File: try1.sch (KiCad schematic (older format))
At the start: 15 parts, among them J10 Archon-connector-modules-Driv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, J11 Archon-connector-modules-Driv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, J2 Archon-connector-modules-Heat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, J21 DB37, J22 DB37, J3 Archon-connector-modules-Driv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, J31 DB9, J4 Archon-connector-modules-LVBi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, J5 Archon-connector-modules-ADC, J6 Archon-connector-modules-ADC, J7 Archon-connector-modules-ADC, J8 Archon-connector-modules-ADC, J9 Archon-connector-modules-HVBi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

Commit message: Finish version 31
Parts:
- gave numbers to parts that had none: 2
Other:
- note added: "Heater"
- note added: "Radiation Shield"
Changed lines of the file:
@@
 $EndComp
 $Comp
-L RJ45_LEDS_SHLD J?
+L RJ45_LEDS_SHLD J41
 U 1 1 5792318E
 P 12800 3250
-F 0 "J?" H 12800 2750 50  0000 C CNN
+F 0 "J41" H 12800 2750 50  0000 C CNN
 F 1 "RJ45_LEDS_SHLD" H 12800 3650 50  0000 C CNN
 F 2 "" H 12800 3200 50  0000 C CNN
@@
 $EndComp
 $Comp
-L RJ45_LEDS_SHLD J?
+L RJ45_LEDS_SHLD J42
 U 1 1 57923203
 P 14900 3250
-F 0 "J?" H 14900 2750 50  0000 C CNN
+F 0 "J42" H 14900 2750 50  0000 C CNN
 F 1 "RJ45_LEDS_SHLD" H 14900 3650 50  0000 C CNN
 F 2 "" H 14900 3200 50  0000 C CNN
@@
 Text Notes 2050 4150 0    60   ~ 0
 LED/Projector
+Text Notes 13700 4200 0    60   ~ 0
+Heater
+Text Notes 13700 4400 0    60   ~ 0
+Radiation Shield
 $EndSCHEMATC

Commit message: Incomplete Wireing (v39)
Switched out RJ45 connectors for DVI.

Partially completed connections.
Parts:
- removed J41, J42: RJ45_LEDS_SHLD, symbol RJ45_LEDS_SHLD
- added J41: CONN_DVI, MODULE, symbol CONN_DVI
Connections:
- net labels added: DRV10_CH1, DRV10_CH2, DRV10_CH3, DRV10_CH4, DRV10_CH5, DRV10_CH6, DRV10_CH7, DRV10_CH8, DRV11_CH1, DRV11_CH2, DRV11_CH3, DRV11_CH4, DRV11_CH5, DRV11_CH6, DRV11_CH7, DRV11_CH8, DRV3_CH1, DRV3_CH2, DRV3_CH3, DRV3_CH4, DRV3_CH5, DRV3_CH6, DRV3_CH7, DRV3_CH8, OUT_LL_GND, OUT_LR_GND, OUT_UL_GND, OUT_UR_GND, OUT__UL_GND
- wire segments 66 -> 92
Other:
- moved on the sheet: J10, J11, J2, J21, J22, J3, J31, J4, J5, J6, J7, J8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

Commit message: Version 41: Partial Wiring
Still very incomplete, but I finished the first pass on wiring.  This
version includes Morley's first pin assignments and some extra changes
we talked about, today.
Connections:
- net labels added: HV9_1, HV9_10, HV9_2, HV9_3, HV9_4, HV9_5, HV9_6, HV9_7, HV9_8, HV9_9, LV4_1, LV4_2, LV4_3, LV4_4, LV4_5, LV4_6, LV4_7, LV4_8, ResetLog_L, ResetLog_R
- net labels removed: ResetLOG_L, ResetLOG_R
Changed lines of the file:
@@
 Title "Archon CCD Camera Controller Interface Board"
 Date "2016-07-08"
-Rev "39"
+Rev "41"
 Comp "Porltand State University"
 Comment1 "Copyright 2016 Paul R. DeStefano"
@@
 ResetHI_L
 Text Label 15450 5300 0    60   ~ 0
-ResetLOG_L
+ResetLog_L
 Text Label 15450 5400 0    60   ~ 0
 VDD_B
@@
 ResetHI_R
 Text Label 12150 5300 0    60   ~ 0
-ResetLOG_R
+ResetLog_R
 Text Label 12150 5400 0    60   ~ 0
 VDD_A
@@
 Text GLabel 12750 3500 2    60   Input ~ 0
 DRV3_CH2
+Text GLabel 22300 11300 0    60   Input ~ 0
+HV9_5
+Text GLabel 22300 11400 0    60   Input ~ 0
+HV9_6
+Text GLabel 22300 11600 0    60   Input ~ 0
+HV9_7
+Text GLabel 22300 11700 0    60   Input ~ 0
+HV9_8
+Text GLabel 22300 11000 0    60   Input ~ 0
+HV9_3
+Text GLabel 22300 11100 0    60   Input ~ 0
+HV9_4
+Text GLabel 22300 10700 0    60   Input ~ 0
+HV9_1
+Text GLabel 22300 10800 0    60   Input ~ 0
+HV9_2
+Text GLabel 16350 5400 2    60   Input ~ 0
+HV9_1
+Text GLabel 16350 5700 2    60   Input ~ 0
+HV9_3
+Text GLabel 16350 5800 2    60   Input ~ 0
+HV9_5
+Text GLabel 16350 6000 2    60   Input ~ 0
+HV9_5
+Text GLabel 12750 5400 2    60   Input ~ 0
+HV9_2
+Text GLabel 12750 5700 2    60   Input ~ 0
+HV9_4
+Text GLabel 12750 5800 2    60   Input ~ 0
+HV9_6
+Text GLabel 12750 6000 2    60   Input ~ 0
+HV9_6
+Text GLabel 12750 5200 2    60   Input ~ 0
+HV9_8
+Text GLabel 16350 5200 2    60   Input ~ 0
+HV9_7
+Text GLabel 8600 10750 0    60   Input ~ 0
+LV4_1
+Text GLabel 8600 10850 0    60   Input ~ 0
+LV4_2
+Text GLabel 8600 11050 0    60   Input ~ 0
+LV4_3
+Text GLabel 8600 11150 0    60   Input ~ 0
+LV4_4
+Text GLabel 8600 11350 0    60   Input ~ 0
+LV4_5
+Text GLabel 8600 11450 0    60   Input ~ 0
+LV4_6
+Text GLabel 8600 11650 0    60   Input ~ 0
+LV4_7
+Text GLabel 8600 11750 0    60   Input ~ 0
+LV4_8
+Text GLabel 16350 5900 2    60   Input ~ 0
+LV4_1
+Text GLabel 12750 5900 2    60   Input ~ 0
+LV4_2
+Text GLabel 16350 5300 2    60   Input ~ 0
+DRV10_CH1
+Text GLabel 12750 5300 2    60   Input ~ 0
+DRV10_CH2
+Text GLabel 16350 4300 2    60   Input ~ 0
+DRV3_CH1
+Text GLabel 12750 4300 2    60   Input ~ 0
+DRV3_CH2
+Text GLabel 16350 4500 2    60   Input ~ 0
+DRV3_CH3
+Text GLabel 12750 4500 2    60   Input ~ 0
+DRV3_CH4
+Text GLabel 16350 4700 2    60   Input ~ 0
+DRV3_CH5
+Text GLabel 12750 4700 2    60   Input ~ 0
+DRV3_CH6
+Text GLabel 16350 4900 2    60   Input ~ 0
+DRV3_CH7
+Text GLabel 12750 4900 2    60   Input ~ 0
+DRV3_CH8
+Text GLabel 16350 6200 2    60   Input ~ 0
+HV9_9
+Text GLabel 12750 6200 2    60   Input ~ 0
+HV9_10
+Text GLabel 22300 11900 0    60   Input ~ 0
+HV9_9
+Text GLabel 22300 12000 0    60   Input ~ 0
+HV9_10
 $EndSCHEMATC

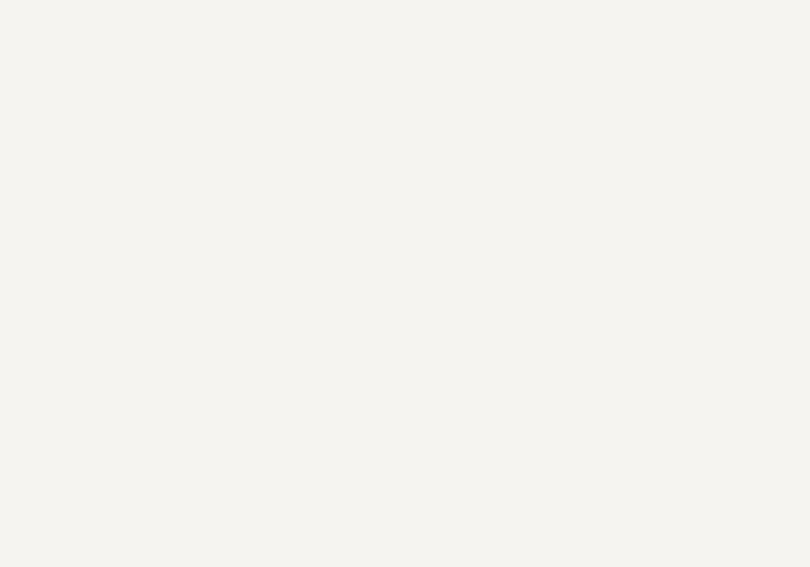
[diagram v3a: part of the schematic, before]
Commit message: Add heater power connector
Added Mini-FiT-Jr 5566 2x2 footprint and connector to hold heater power
connections to cold finger heater and radiation shield heater.
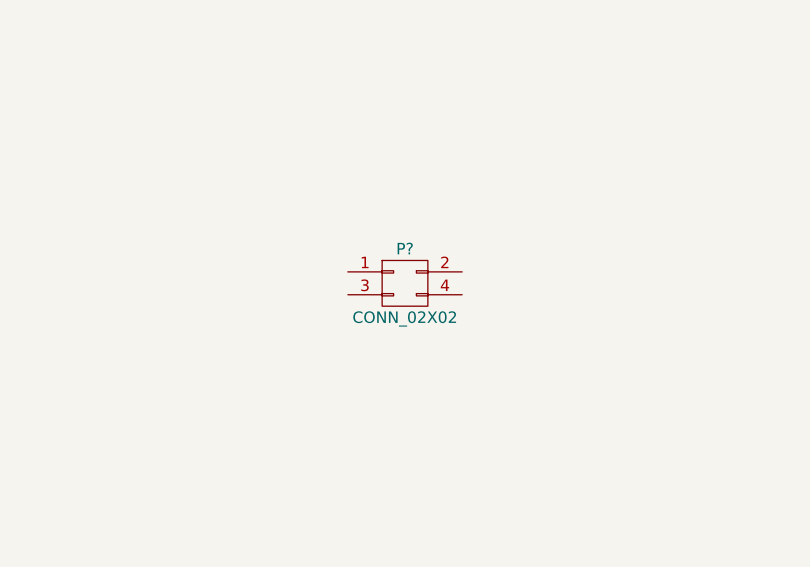
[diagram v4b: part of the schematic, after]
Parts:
- added P?: CONN_02X02, symbol CONN_02X02
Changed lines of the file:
@@
 Text GLabel 22300 12000 0    60   Input ~ 0
 HV9_10
+$Comp
+L CONN_02X02 P?
+U 1 1 57B547B3
+P 20850 4650
+F 0 "P?" H 20850 4800 50  0000 C CNN
+F 1 "CONN_02X02" H 20850 4500 50  0000 C CNN
+F 2 "" H 20850 3450 50  0000 C CNN
+F 3 "" H 20850 3450 50  0000 C CNN
+	1    20850 4650
+	1    0    0    -1
+$EndComp
 $EndSCHEMATC

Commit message: Connect heater/DVI, label shutter connector
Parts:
- added W? (x6): TEST_1P, symbol TEST_1P
- P?: footprint (none) -> ccdcamera:Molex_MiniFit-JR-5556-04B_2x02x4.20mm_Straight
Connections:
- net labels added: DVI_P9_SPARET1, DVI_P9_SPARET2, DVI_P9_SPARET3, DVI_P9_SPARET4, DVI_P9_SPARET5, DVI_P9_SPARET6, DVI_P9_T1, DVI_P9_T2, DVI_P9_T3, DVI_P9_T4, DVI_P9_T5, DVI_P9_T6, FLASH_V, HEATER1_AN, HEATER1_AP, HEATER1_BN, HEATER1_BP, HEATER1_TEMPA_FN, HEATER1_TEMPA_FP, HEATER1_TEMPA_SN, HEATER1_TEMPA_SP, HEATER1_TEMPB_FN, HEATER1_TEMPB_FP, HEATER1_TEMPB_SN, HEATER1_TEMPB_SP, SEL_LED_1, SEL_LED_2, SHUT_+15V, SHUT_+5, SHUT_OUT, ~FLASH_STB
- net labels removed: OUT__UL_GND
- wire segments 92 -> 66
- no-connect marks 26 -> 43
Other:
- note added: "LED/Projector\n(Formerly J73 - Shutter Control)"
- note added: "SHIELD PINS:\n3,11,19,22"
- note removed: "LED/Projector"

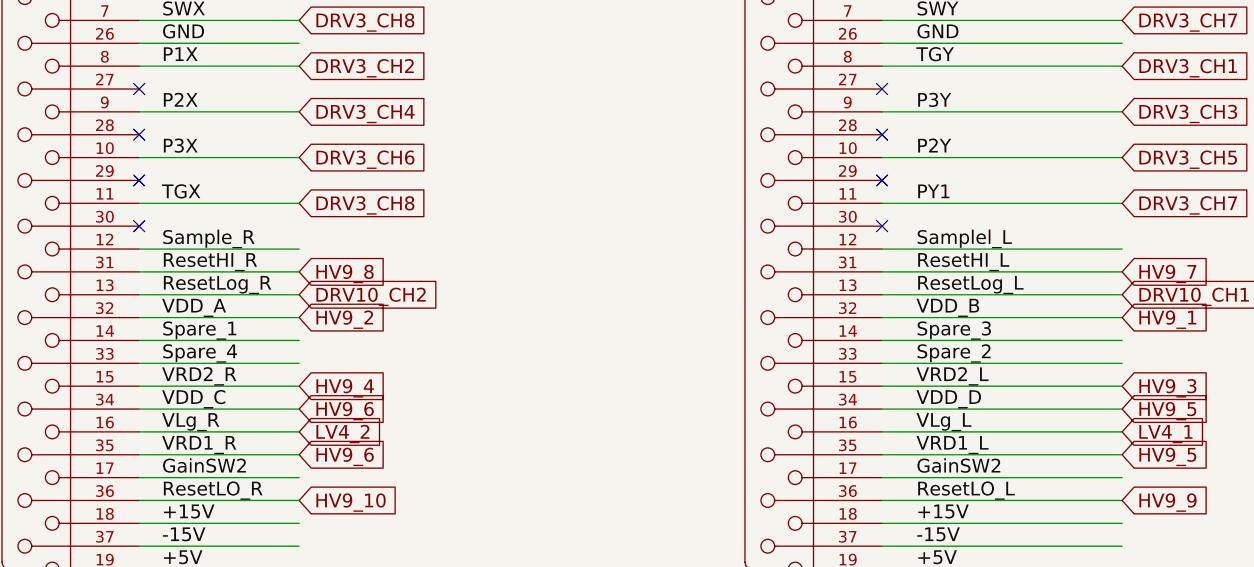
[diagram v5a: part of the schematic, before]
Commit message: schematic: chg ResetHI_L/R to ~(not) logic
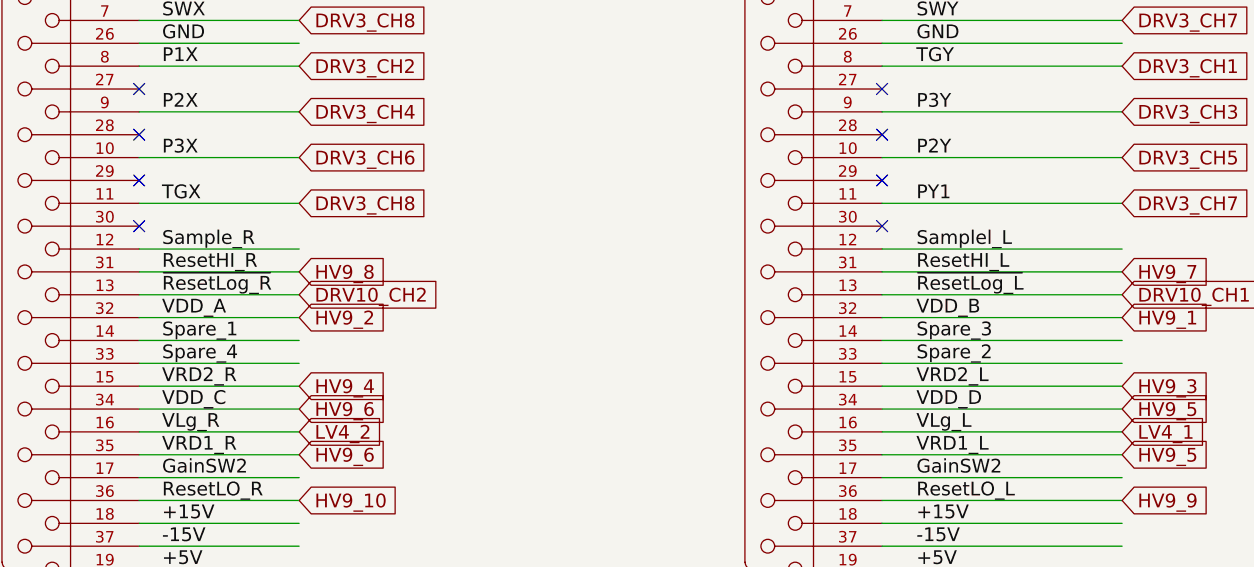
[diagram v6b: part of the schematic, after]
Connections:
- net labels added: ~ResetLog_L, ~ResetLog_R
- net labels removed: ResetLog_L, ResetLog_R
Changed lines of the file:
@@
 ResetHI_L
 Text Label 15450 5300 0    60   ~ 0
-ResetLog_L
+~ResetLog_L
 Text Label 15450 5400 0    60   ~ 0
 VDD_B
@@
 ResetHI_R
 Text Label 12150 5300 0    60   ~ 0
-ResetLog_R
+~ResetLog_R
 Text Label 12150 5400 0    60   ~ 0
 VDD_A

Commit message: fill with non-connects
Added non-connect flags for all unassinged pins.
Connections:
- net labels added: DRV3_GND1, DRV3_GND2
- no-connect marks 43 -> 310
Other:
- moved on the sheet: J7, J8

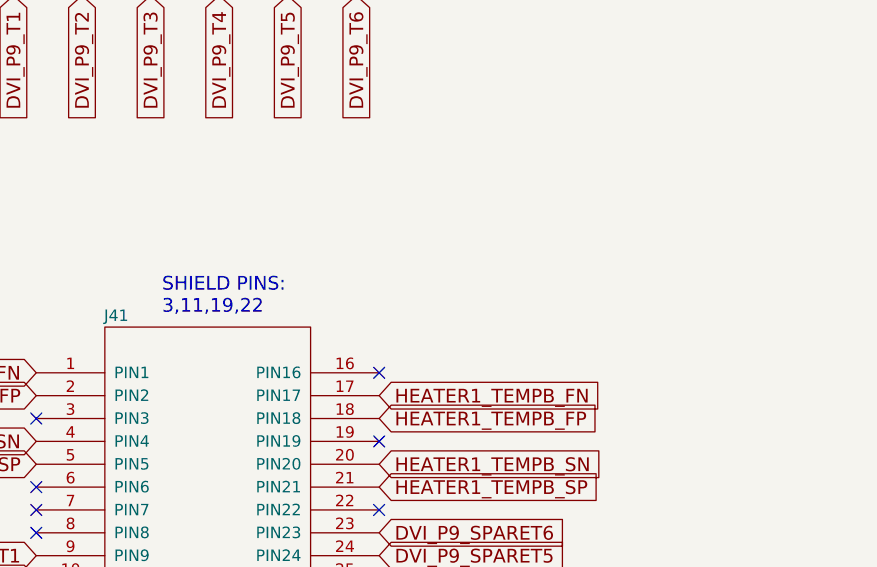
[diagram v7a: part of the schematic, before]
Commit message: Update comment for DVI connector re:shield pins
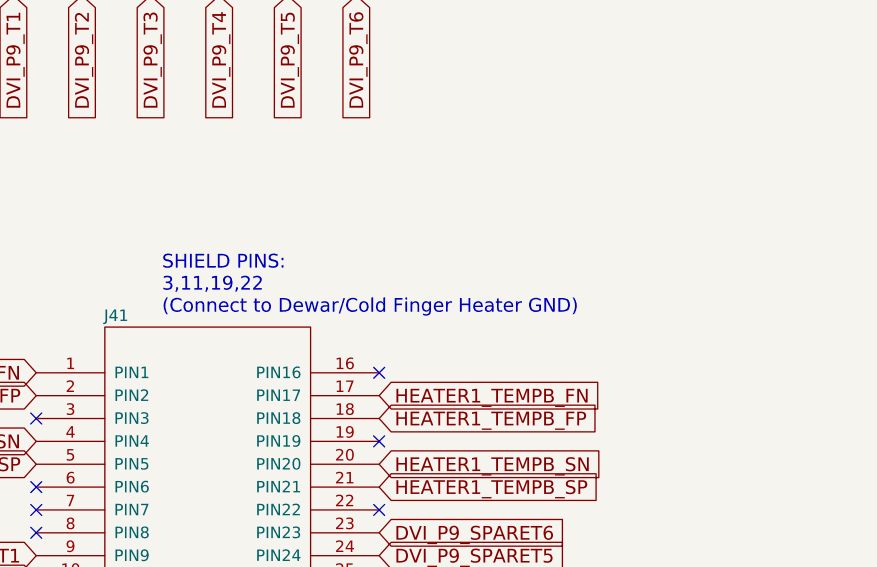
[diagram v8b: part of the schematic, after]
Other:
- note added: "SHIELD PINS:\n3,11,19,22\n(Connect to Dewar/Cold Finger Heater GND)"
- note removed: "SHIELD PINS:\n3,11,19,22"
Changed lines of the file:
@@
 DVI_P9_T6
 Text Notes 23300 3900 0    60   ~ 0
-SHIELD PINS:\n3,11,19,22
+SHIELD PINS:\n3,11,19,22\n(Connect to Dewar/Cold Finger Heater GND)
 NoConn ~ 22750 4350
 NoConn ~ 22750 5150
